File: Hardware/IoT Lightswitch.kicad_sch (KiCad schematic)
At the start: 23 parts, among them J1 Screw_Terminal_01x04, J2 Conn_01x04, K1 SANYOU_SRD_Form_C, Q1 NMOS, SW1 SW_SPDT, SW2 SW_SPDT, SW3 SW_Push, SW4 SW_Push, SW5 SW_SPST, U1 ESP32-S2-SOLO-2

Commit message: Updated Schema
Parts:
- C2: Rating (none) -> 250v
- F1: value Fuse -> 5A 250v
- F3: value Fuse -> 0.5A 125v
- R2: value R -> 10k
- R3: value R_Small -> 10k
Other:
- moved on the sheet: C2, PS1, RV1, U1

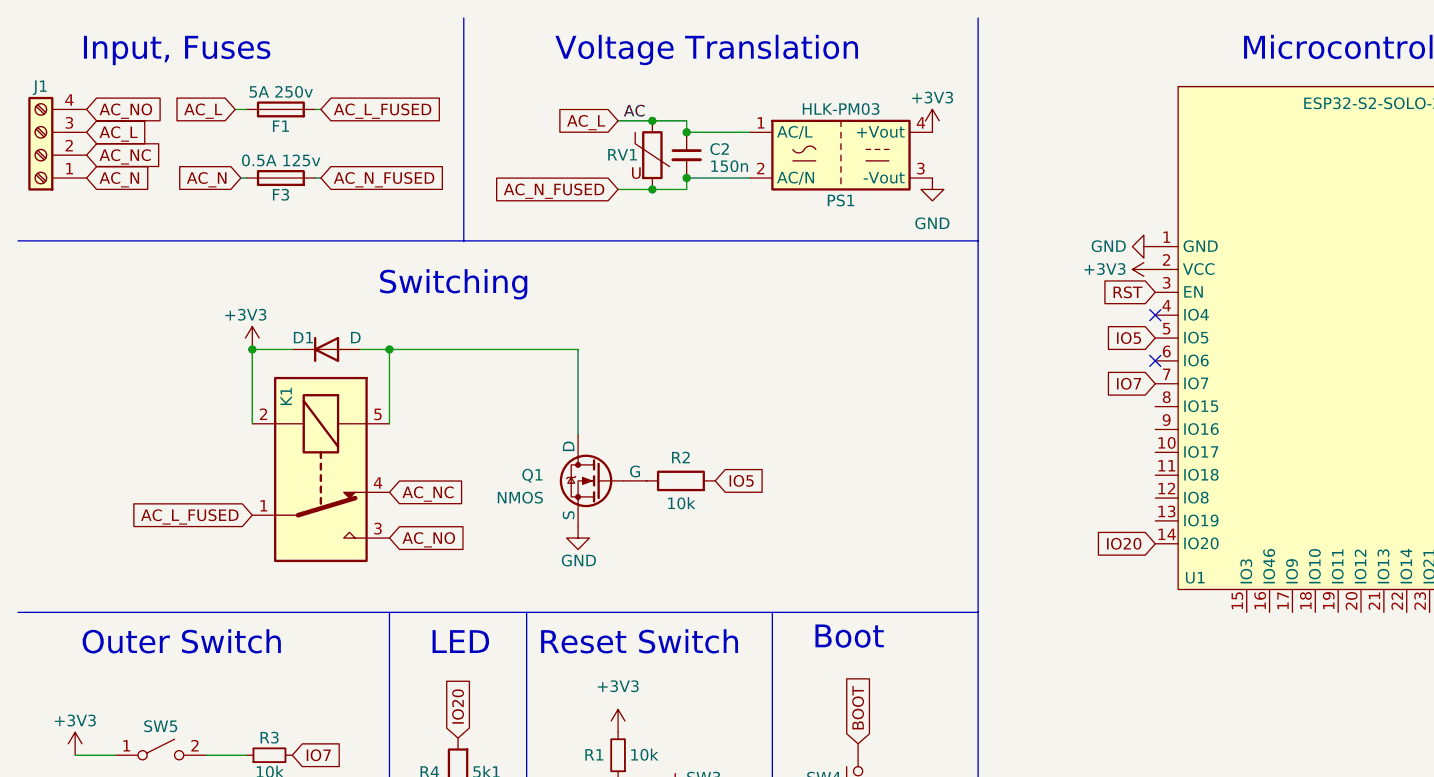
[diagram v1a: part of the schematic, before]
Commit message: Moved PSU Fuse from Neutral to Live
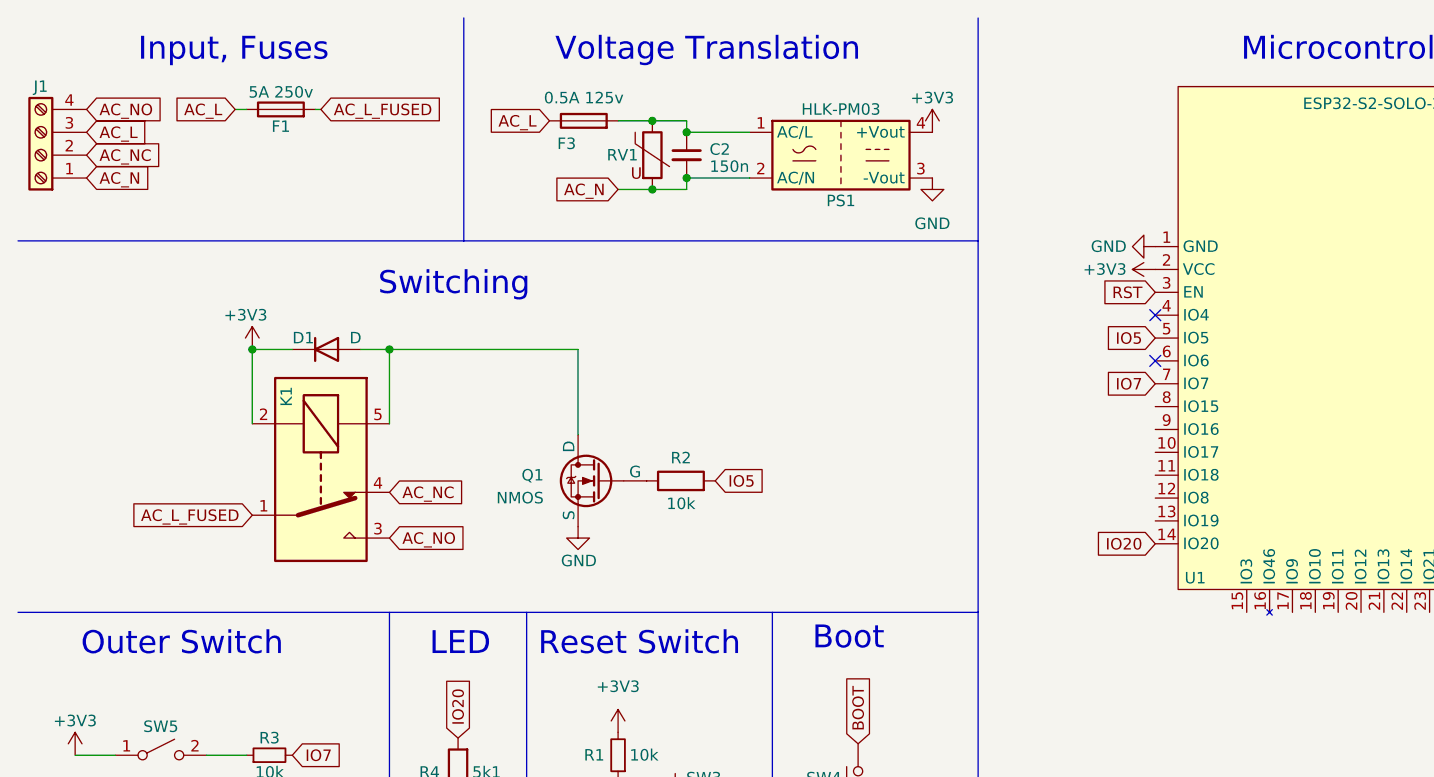
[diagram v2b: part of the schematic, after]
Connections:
- net AC_L: now also F3.1; no longer C2.1, PS1.1 (AC/L), RV1.1
- net AC_N: now also C2.2, PS1.2 (AC/N), RV1.2; no longer F3.1
- removed net AC_N_FUSED: C2.2, F3.2, PS1.2 (AC/N), RV1.2
- new net: C2.1, F3.2, PS1.1 (AC/L), RV1.1
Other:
- moved on the sheet: F3
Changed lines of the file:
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@@
-    (stroke (width 0) (type default))
-  )
-  (wire (pts (xy 45.72 30.48) (xy 46.355 30.48))
     (stroke (width 0) (type default))
   )
@@
     (stroke (width 0) (type default))
   )
-  (wire (pts (xy 37.465 30.48) (xy 38.1 30.48))
-    (stroke (width 0) (type default))
-  )
   (wire (pts (xy 187.325 35.56) (xy 187.96 35.56))
     (stroke (width 0) (type default))
@@
     (effects (font (size 2.54 2.54)) (justify left bottom))
   )
-  (text "Input, Fuses" (at 19.685 17.78 0)
+  (text "Input, Fuses" (at 26.035 17.78 0)
     (effects (font (size 2.54 2.54)) (justify left bottom))
   )
@@
   (text "Voltage Translation" (at 72.39 17.78 0)
     (effects (font (size 2.54 2.54)) (justify left bottom))
-  )
-  (label "AC" (at 80.01 24.13 0) (fields_autoplaced)
-    (effects (font (size 1.27 1.27)) (justify left bottom))
   )
   (label "AC_B" (at 387.35 240.03 0) (fields_autoplaced)
@@
     )
   )
+  (global_label "AC_N" (shape input) (at 79.375 31.75 180) (fields_autoplaced)
+    (effects (font (size 1.27 1.27)) (justify right))
+    (property "Intersheetrefs" "${INTERSHEET_REFS}" (at 71.8125 31.75 0)
+      (effects (font (size 1.27 1.27)) (justify right) hide)
+    )
+  )
   (global_label "LIVE" (shape input) (at 376.555 237.49 180) (fields_autoplaced)
     (effects (font (size 1.27 1.27)) (justify right))
@@
     )
   )
-  (global_label "AC_N" (shape input) (at 37.465 30.48 180) (fields_autoplaced)
-    (effects (font (size 1.27 1.27)) (justify right))
-    (property "Intersheetrefs" "${INTERSHEET_REFS}" (at 29.9025 30.48 0)
-      (effects (font (size 1.27 1.27)) (justify right) hide)
-    )
-  )
   (global_label "AC_NC" (shape input) (at 53.975 65.405 0) (fields_autoplaced)
     (effects (font (size 1.27 1.27)) (justify left))
@@
     )
   )
-  (global_label "AC_N_FUSED" (shape input) (at 79.375 31.75 180) (fields_autoplaced)
-    (effects (font (size 1.27 1.27)) (justify right))
-    (property "Intersheetrefs" "${INTERSHEET_REFS}" (at 64.7973 31.75 0)
-      (effects (font (size 1.27 1.27)) (justify right) hide)
-    )
-  )
   (global_label "TX" (shape input) (at 384.81 27.94 180) (fields_autoplaced)
     (effects (font (size 1.27 1.27)) (justify right))
@@
     )
   )
-  (global_label "AC_N_FUSED" (shape input) (at 46.355 30.48 0) (fields_autoplaced)
-    (effects (font (size 1.27 1.27)) (justify left))
-    (property "Intersheetrefs" "${INTERSHEET_REFS}" (at 60.9327 30.48 0)
-      (effects (font (size 1.27 1.27)) (justify left) hide)
-    )
-  )
   (global_label "AC_NC" (shape input) (at 20.32 27.94 0) (fields_autoplaced)
     (effects (font (size 1.27 1.27)) (justify left))
@@
     )
   )
-  (global_label "AC_L" (shape input) (at 79.375 24.13 180) (fields_autoplaced)
-    (effects (font (size 1.27 1.27)) (justify right))
-    (property "Intersheetrefs" "${INTERSHEET_REFS}" (at 72.1149 24.13 0)
+  (global_label "AC_L" (shape input) (at 71.755 24.13 180) (fields_autoplaced)
+    (effects (font (size 1.27 1.27)) (justify right))
+    (property "Intersheetrefs" "${INTERSHEET_REFS}" (at 64.4949 24.13 0)
       (effects (font (size 1.27 1.27)) (justify right) hide)
     )
@@
     )
   )
-  (symbol (lib_id "Device:Fuse") (at 41.91 30.48 90) (unit 1)
+  (symbol (lib_id "Device:Fuse") (at 75.565 24.13 90) (unit 1)
     (in_bom yes) (on_board yes) (dnp no)
-    (property "Reference" "F3" (at 41.91 32.385 90)
-      (effects (font (size 1.27 1.27)))
-    )
-    (property "Value" "0.5A 125v" (at 41.91 28.575 90)
-      (effects (font (size 1.27 1.27)))
-    )
-    (property "Footprint" "6125_Fuse:Fuse_6125" (at 41.91 32.258 90)
-      (effects (font (size 1.27 1.27)) hide)
-    )
-    (property "Datasheet" "~" (at 41.91 30.48 0)
-      (effects (font (size 1.27 1.27)) hide)
-    )
+    (property "Reference" "F3" (at 73.66 26.67 90)
+      (effects (font (size 1.27 1.27)))
+    )
+    (property "Value" "0.5A 125v" (at 75.565 21.59 90)
+      (effects (font (size 1.27 1.27)))
+    )
+    (property "Footprint" "6125_Fuse:Fuse_6125" (at 75.565 25.908 90)
+      (effects (font (size 1.27 1.27)) hide)
+    )
+    (property "Datasheet" "~" (at 75.565 24.13 0)
+      (effects (font (size 1.27 1.27)) hide)
+    )
